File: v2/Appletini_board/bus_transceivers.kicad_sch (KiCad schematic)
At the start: 23 parts, among them U10 74AHC1G126, U11 SN74LVC1G14DBV, U13 74LVC1G08, U3 SN74LVC543ADW, U4 SN74LVC543ADW, U5 SN74LVC543ADW, U6 SN74LVC543ADW, U7 TXS0108EPW, U8 74LCX07, U9 74AHC1G126

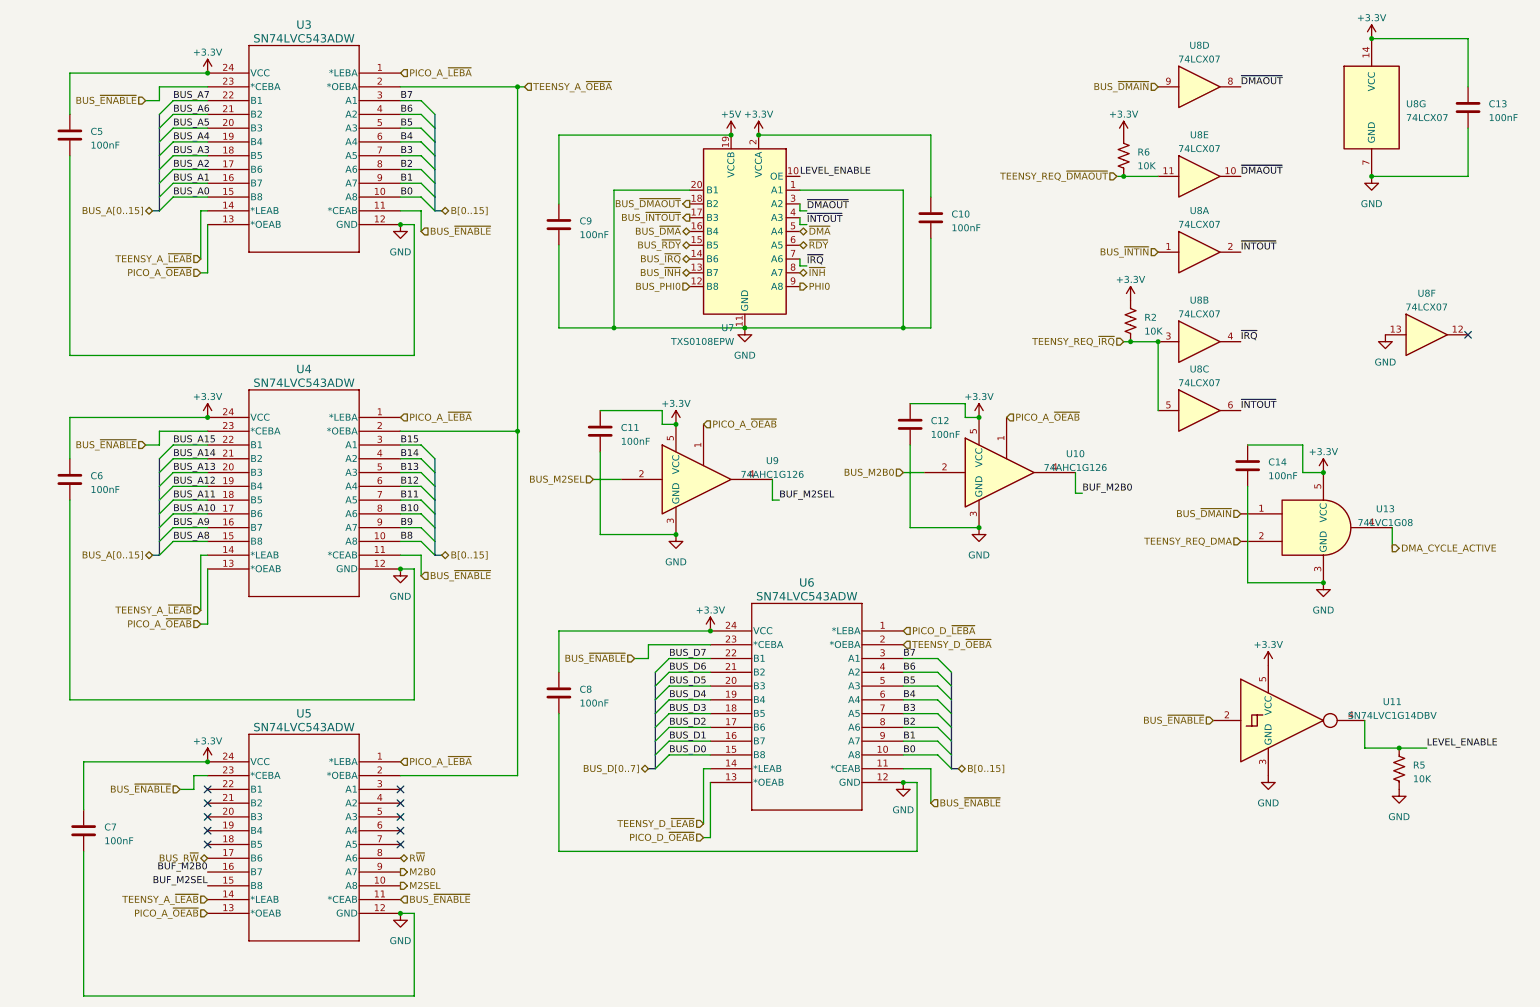
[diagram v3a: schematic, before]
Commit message: board ordered
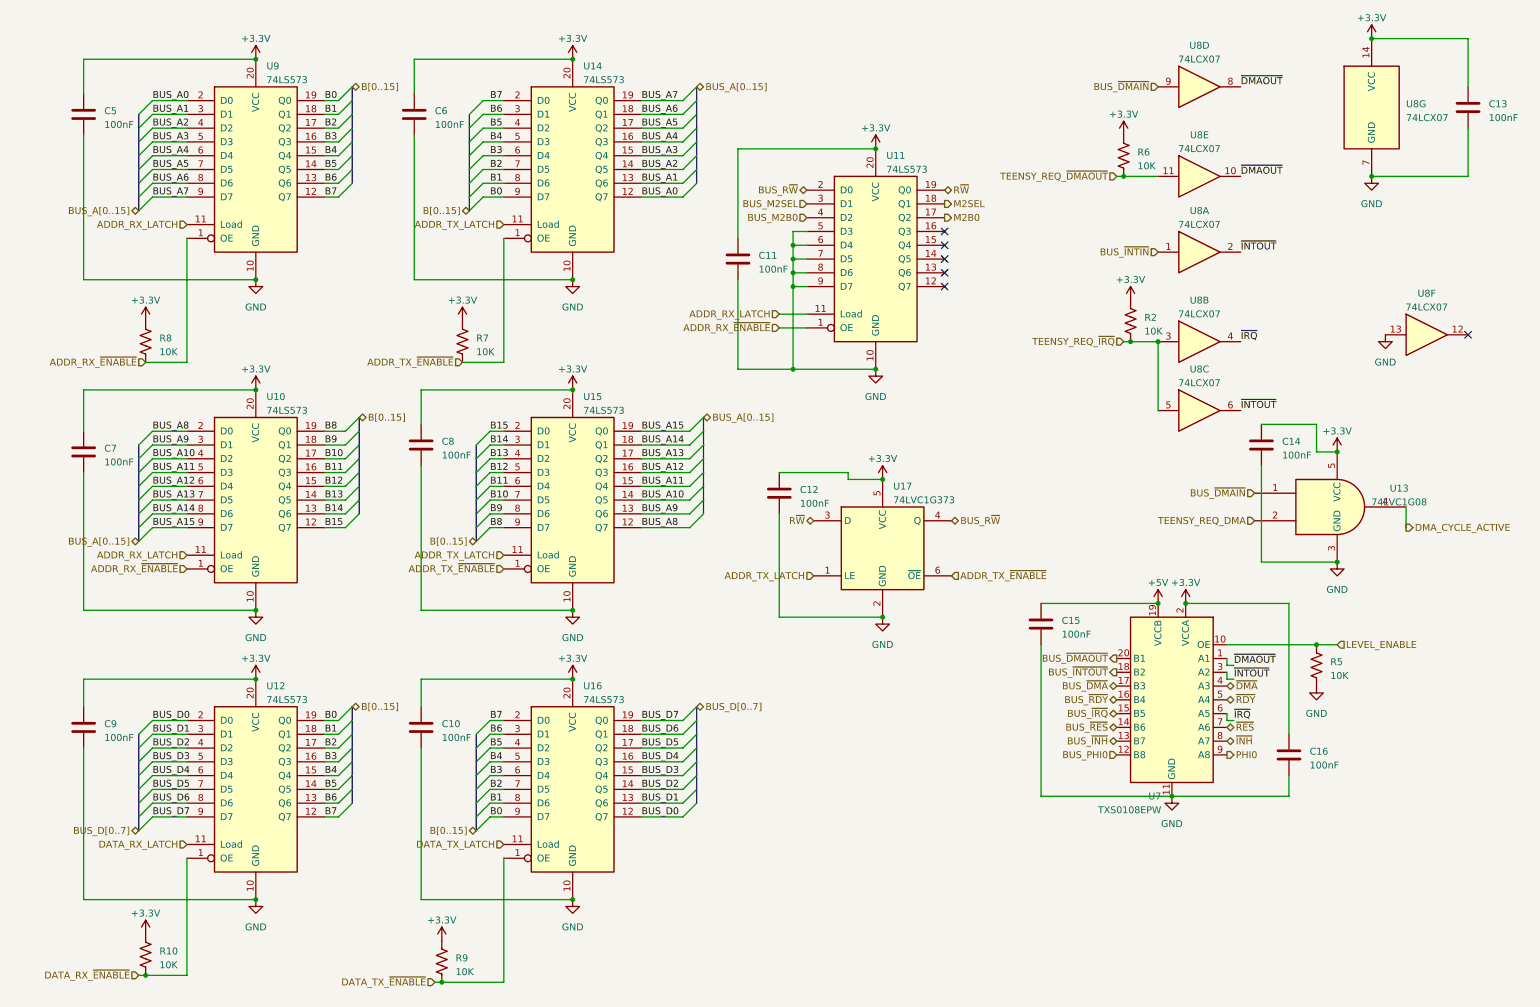
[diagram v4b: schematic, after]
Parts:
- removed U10, U9: 74AHC1G126, Package_TO_SOT_SMD:SOT-23-5, symbol 74xGxx:74AHC1G126
- removed U11: SN74LVC1G14DBV, Package_TO_SOT_SMD:SOT-23-5, symbol 74xGxx:SN74LVC1G14DBV
- removed U3, U4, U5, U6: SN74LVC543ADW, Package_SO:SSOP-24_5.3x8.2mm_P0.65mm, symbol 74lvc543:SN74LVC543ADW
- added C10, C9: 100nF, Capacitor_SMD:C_1206_3216Metric, symbol Device:C
- added R10, R7, R8, R9: 10K, Resistor_SMD:R_0402_1005Metric, symbol Device:R_US
- added U10, U11, U12, U14, U15, U16, U9: 74LS573, Package_SO:TSSOP-20_4.4x6.5mm_P0.65mm, symbol 74xx:74LS573
- added U17: 74LVC1G373, Package_TO_SOT_SMD:SOT-23-6, symbol 74xGxx:74LVC1G373
- C11, C12, C5, C6, C7, C8: LCSC C24497 -> (none)
- R5: LCSC C2991755 -> (none)
- renumbered C9 to C15, C10 to C16
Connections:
- net +3.3V: now also C10.1, C9.1, R10.1, R7.1, R8.1, R9.1, U10.20 (VCC), U11.20 (VCC), U12.20 (VCC), U14.20 (VCC), U15.20 (VCC), U16.20 (VCC), U17.5 (VCC), U9.20 (VCC)
- net B0: now also U12.19 (Q0), U14.9 (D7), U16.9 (D7), U9.19 (Q0)
- net B1: now also U12.18 (Q1), U14.8 (D6), U16.8 (D6), U9.18 (Q1)
- net B10: now also U10.17 (Q2), U15.7 (D5)
- net B11: now also U10.16 (Q3), U15.6 (D4)
- net B12: now also U10.15 (Q4), U15.5 (D3)
- net B13: now also U10.14 (Q5), U15.4 (D2)
- net B14: now also U10.13 (Q6), U15.3 (D1)
- net B15: now also U10.12 (Q7), U15.2 (D0)
- net B2: now also U12.17 (Q2), U14.7 (D5), U16.7 (D5), U9.17 (Q2)
- net B3: now also U12.16 (Q3), U14.6 (D4), U16.6 (D4), U9.16 (Q3)
- net B4: now also U12.15 (Q4), U14.5 (D3), U16.5 (D3), U9.15 (Q4)
- net B5: now also U12.14 (Q5), U14.4 (D2), U16.4 (D2), U9.14 (Q5)
- net B6: now also U12.13 (Q6), U14.3 (D1), U16.3 (D1), U9.13 (Q6)
- net B7: now also U12.12 (Q7), U14.2 (D0), U16.2 (D0), U9.12 (Q7)
- net B8: now also U10.19 (Q0), U15.9 (D7)
- net B9: now also U10.18 (Q1), U15.8 (D6)
- net BUS_A0: now also U14.12 (Q7), U9.2 (D0)
- net BUS_A1: now also U14.13 (Q6), U9.3 (D1)
- net BUS_A10: now also U10.4 (D2), U15.14 (Q5)
- net BUS_A11: now also U10.5 (D3), U15.15 (Q4)
- net BUS_A12: now also U10.6 (D4), U15.16 (Q3)
- net BUS_A13: now also U10.7 (D5), U15.17 (Q2)
- net BUS_A14: now also U10.8 (D6), U15.18 (Q1)
- net BUS_A15: now also U10.9 (D7), U15.19 (Q0)
- net BUS_A2: now also U14.14 (Q5), U9.4 (D2)
- net BUS_A3: now also U14.15 (Q4), U9.5 (D3)
- net BUS_A4: now also U14.16 (Q3), U9.6 (D4)
- net BUS_A5: now also U14.17 (Q2), U9.7 (D5)
- net BUS_A6: now also U14.18 (Q1), U9.8 (D6)
- net BUS_A7: now also U14.19 (Q0), U9.9 (D7)
- net BUS_A8: now also U10.2 (D0), U15.12 (Q7)
- net BUS_A9: now also U10.3 (D1), U15.13 (Q6)
- net BUS_D0: now also U12.2 (D0), U16.12 (Q7)
- net BUS_D1: now also U12.3 (D1), U16.13 (Q6)
- net BUS_D2: now also U12.4 (D2), U16.14 (Q5)
- net BUS_D3: now also U12.5 (D3), U16.15 (Q4)
- net BUS_D4: now also U12.6 (D4), U16.16 (Q3)
- net BUS_D5: now also U12.7 (D5), U16.17 (Q2)
- net BUS_D6: now also U12.8 (D6), U16.18 (Q1)
- net BUS_D7: now also U12.9 (D7), U16.19 (Q0)
- net BUS_M2B0: now also U11.4 (D2)
- net BUS_M2SEL: now also U11.3 (D1)
- net BUS_R~{W}: now also U11.2 (D0), U17.4 (Q)
- net BUS_~{DMAOUT}: now also U7.20 (B1); no longer U7.18 (B2)
- net BUS_~{DMA}: now also U7.17 (B3); no longer U7.16 (B4)
- net BUS_~{INTOUT}: now also U7.18 (B2); no longer U7.17 (B3)
- net BUS_~{IRQ}: now also U7.15 (B5); no longer U7.14 (B6)
- net BUS_~{RDY}: now also U7.16 (B4); no longer U7.15 (B5)
- net GND: now also C10.2, C9.2, U10.10 (GND), U11.10 (GND), U11.5 (D3), U11.6 (D4), U11.7 (D5), U11.8 (D6), U11.9 (D7), U12.10 (GND), U14.10 (GND), U15.10 (GND), U16.10 (GND), U17.2 (GND), U9.10 (GND); no longer U7.1 (A1), U7.20 (B1)
- net M2B0: now also U11.17 (Q2)
- net M2SEL: now also U11.18 (Q1)
- net R~{W}: now also U11.19 (Q0), U17.3 (D)
- net ~{DMAOUT}: now also U7.1 (A1); no longer U7.3 (A2)
- net ~{DMA}: now also U7.4 (A3); no longer U7.5 (A4)
- net ~{INTOUT}: now also U7.3 (A2); no longer U7.4 (A3)
- net ~{IRQ}: now also U7.6 (A5); no longer U7.7 (A6)
- net ~{RDY}: now also U7.5 (A4); no longer U7.6 (A5)
- new net ADDR_RX_LATCH: U10.11 (Load), U11.11 (Load), U9.11 (Load)
- new net ADDR_RX_~{ENABLE}: R8.2, U10.1 (OE), U11.1 (OE), U9.1 (OE)
- new net ADDR_TX_LATCH: U14.11 (Load), U15.11 (Load), U17.1 (LE)
- new net ADDR_TX_~{ENABLE}: R7.2, U14.1 (OE), U15.1 (OE), U17.6 (~{OE})
- new net BUS_~{RES}: U7.14 (B6)
- new net DATA_RX_LATCH: U12.11 (Load)
- new net DATA_RX_~{ENABLE}: R10.2, U12.1 (OE)
- new net DATA_TX_LATCH: U16.11 (Load)
- new net DATA_TX_~{ENABLE}: R9.2, U16.1 (OE)
- new net ~{RES}: U7.7 (A6)
- no-connect marks 11 -> 6
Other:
- moved on the sheet: C14, C15, C16, U13, U7
